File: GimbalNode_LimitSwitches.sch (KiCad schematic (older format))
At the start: 22 parts, among them P4 CONN_01X08_2MNT, P5 CONN_01X08_2MNT, U10 MAX3232CDR, U7 MAX3232CDR, U8 MAX3232CDR, U9 MAX3232CDR

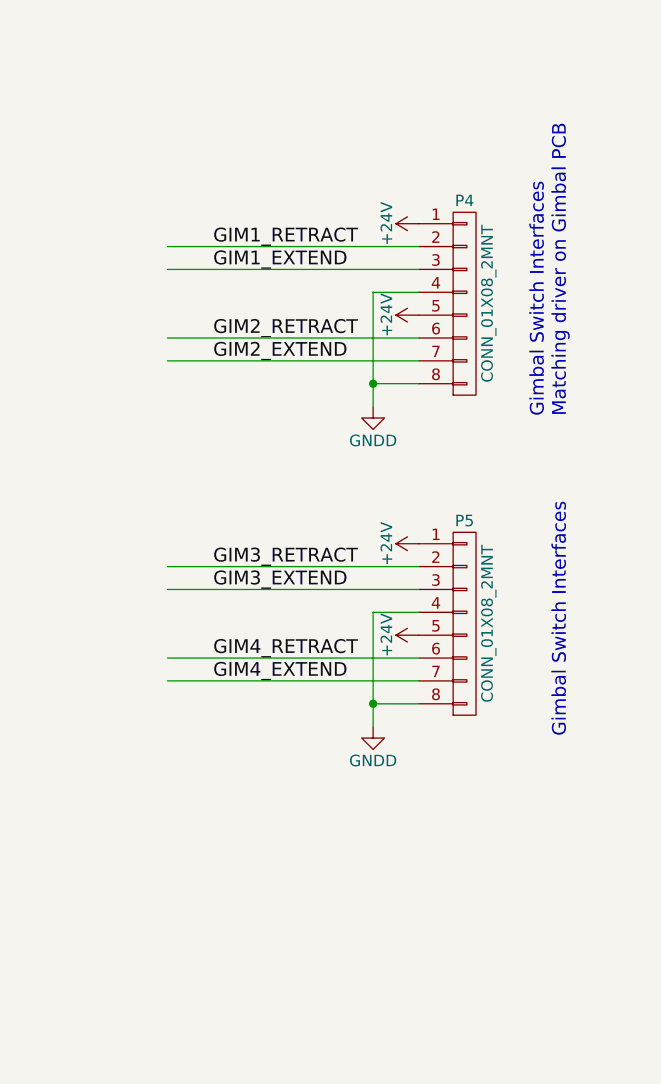
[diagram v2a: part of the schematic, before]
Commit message: Update connectors, diodes, add zener's and anotate.
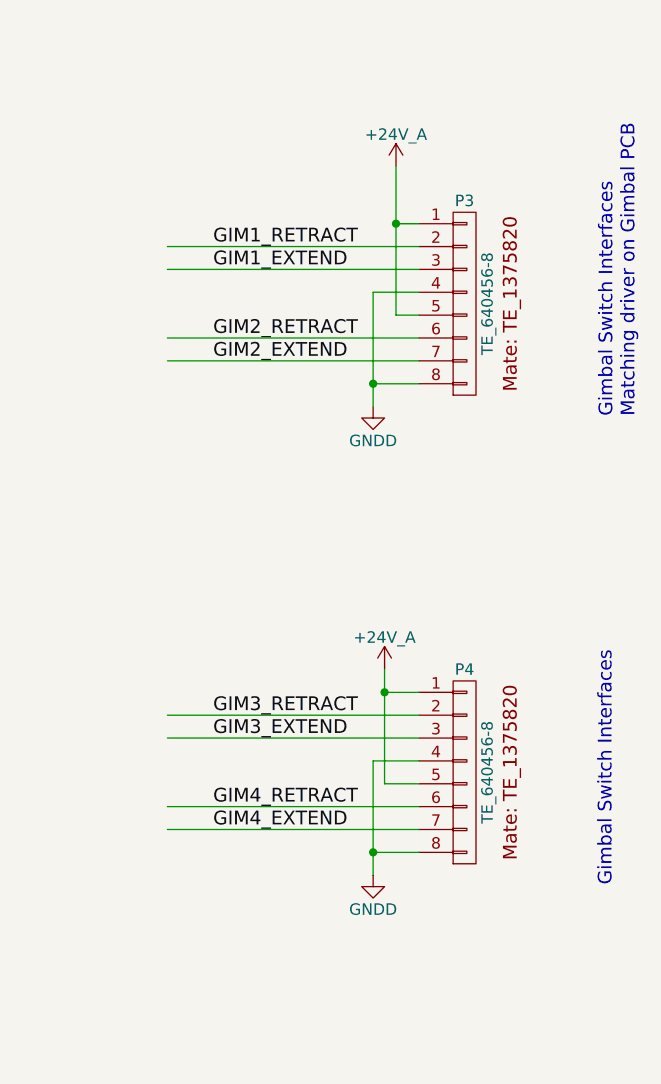
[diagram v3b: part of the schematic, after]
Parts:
- removed P4, P5: CONN_01X08_2MNT, symbol CONN_01X08_2MNT
- added P3, P4: TE_640456-8, RLOOP_FOOTPRINTS:rLoop_TE640456-8, symbol TE_640456-8
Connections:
- net labels added: +24V_A
- net labels removed: +24V
- wire segments 74 -> 80
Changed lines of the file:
@@
 $Descr A3 16535 11693
 encoding utf-8
-Sheet 5 6
+Sheet 4 6
 Title "Gimbal Switch Interface"
 Date ""
@@
 GIM1_EXTEND
 $Comp
-L GNDD #PWR66
+L GNDD #PWR046
 U 1 1 5757EC67
 P 3500 4650
-F 0 "#PWR66" H 3500 4400 50  0001 C CNN
+F 0 "#PWR046" H 3500 4400 50  0001 C CNN
 F 1 "GNDD" H 3500 4500 50  0000 C CNN
 F 2 "" H 3500 4650 50  0000 C CNN
@@
 	3850 4650 3850 4350
 $Comp
-L +3V3_A #PWR65
+L +3V3_A #PWR047
 U 1 1 5757EC68
 P 3500 2000
-F 0 "#PWR65" H 3500 1850 50  0001 C CNN
+F 0 "#PWR047" H 3500 1850 50  0001 C CNN
 F 1 "+3V3_A" H 3500 2140 50  0000 C CNN
 F 2 "" H 3500 2000 60  0000 C CNN
@@
 	2750 3200 2750 3000
 $Comp
-L GNDD #PWR63
+L GNDD #PWR048
 U 1 1 5757EC69
 P 3150 3450
-F 0 "#PWR63" H 3150 3200 50  0001 C CNN
+F 0 "#PWR048" H 3150 3200 50  0001 C CNN
 F 1 "GNDD" H 3150 3300 50  0000 C CNN
 F 2 "" H 3150 3450 50  0000 C CNN
@@
 Wire Wire Line
 	3150 3450 3150 3550
-$Comp
-L CONN_01X08_2MNT P4
-U 1 1 5757EC6A
-P 14300 1850
-F 0 "P4" H 14300 2300 50  0000 C CNN
-F 1 "CONN_01X08_2MNT" V 14400 1850 50  0000 C CNN
-F 2 "" H 14300 1850 50  0000 C CNN
-F 3 "" H 14300 1850 50  0000 C CNN
-	1    14300 1850
-	1    0    0    -1
-$EndComp
-Text Notes 14750 2350 1    60   ~ 0
+Text Notes 15050 2350 1    60   ~ 0
 Gimbal Switch Interfaces\nMatching driver on Gimbal PCB
 $Comp
-L +24V #PWR77
-U 1 1 5757EC6B
-P 14100 1500
-F 0 "#PWR77" H 14100 1350 50  0001 C CNN
-F 1 "+24V" H 14100 1640 50  0000 C CNN
-F 2 "" H 14100 1500 50  0000 C CNN
-F 3 "" H 14100 1500 50  0000 C CNN
-	1    14100 1500
-	0    -1   -1   0
-$EndComp
-$Comp
-L +24V #PWR78
-U 1 1 5757EC6C
-P 14100 1900
-F 0 "#PWR78" H 14100 1750 50  0001 C CNN
-F 1 "+24V" H 14100 2040 50  0000 C CNN
-F 2 "" H 14100 1900 50  0000 C CNN
-F 3 "" H 14100 1900 50  0000 C CNN
-	1    14100 1900
-	0    -1   -1   0
-$EndComp
-$Comp
-L GNDD #PWR75
+L GNDD #PWR049
 U 1 1 5757EC6D
 P 13900 2300
-F 0 "#PWR75" H 13900 2050 50  0001 C CNN
+F 0 "#PWR049" H 13900 2050 50  0001 C CNN
 F 1 "GNDD" H 13900 2150 50  0000 C CNN
 F 2 "" H 13900 2300 50  0000 C CNN
@@
 Text Label 13200 2100 0    60   ~ 0
 GIM2_EXTEND
-$Comp
-L CONN_01X08_2MNT P5
-U 1 1 5757EC6E
-P 14300 3250
-F 0 "P5" H 14300 3700 50  0000 C CNN
-F 1 "CONN_01X08_2MNT" V 14400 3250 50  0000 C CNN
-F 2 "" H 14300 3250 50  0000 C CNN
-F 3 "" H 14300 3250 50  0000 C CNN
-	1    14300 3250
-	1    0    0    -1
-$EndComp
-Text Notes 14750 3750 1    60   ~ 0
+Text Notes 14950 4400 1    60   ~ 0
 Gimbal Switch Interfaces
 $Comp
-L +24V #PWR79
-U 1 1 5757EC6F
-P 14100 2900
-F 0 "#PWR79" H 14100 2750 50  0001 C CNN
-F 1 "+24V" H 14100 3040 50  0000 C CNN
-F 2 "" H 14100 2900 50  0000 C CNN
-F 3 "" H 14100 2900 50  0000 C CNN
-	1    14100 2900
-	0    -1   -1   0
-$EndComp
-$Comp
-L +24V #PWR80
-U 1 1 5757EC70
-P 14100 3300
-F 0 "#PWR80" H 14100 3150 50  0001 C CNN
-F 1 "+24V" H 14100 3440 50  0000 C CNN
-F 2 "" H 14100 3300 50  0000 C CNN
-F 3 "" H 14100 3300 50  0000 C CNN
-	1    14100 3300
-	0    -1   -1   0
-$EndComp
-$Comp
-L GNDD #PWR76
+L GNDD #PWR050
 U 1 1 5757EC71
-P 13900 3700
-F 0 "#PWR76" H 13900 3450 50  0001 C CNN
-F 1 "GNDD" H 13900 3550 50  0000 C CNN
-F 2 "" H 13900 3700 50  0000 C CNN
-F 3 "" H 13900 3700 50  0000 C CNN
-	1    13900 3700
-	1    0    0    -1
-$EndComp
-Wire Wire Line
-	14100 3200 13900 3200
-Wire Wire Line
-	13900 3200 13900 3700
-Wire Wire Line
-	14100 3600 13900 3600
-Connection ~ 13900 3600
-Wire Wire Line
-	13000 3000 14100 3000
-Text Label 13200 3000 0    60   ~ 0
+P 13900 4350
+F 0 "#PWR050" H 13900 4100 50  0001 C CNN
+F 1 "GNDD" H 13900 4200 50  0000 C CNN
+F 2 "" H 13900 4350 50  0000 C CNN
+F 3 "" H 13900 4350 50  0000 C CNN
+	1    13900 4350
+	1    0    0    -1
+$EndComp
+Wire Wire Line
+	14100 3850 13900 3850
+Wire Wire Line
+	13900 3850 13900 4350
+Wire Wire Line
+	14100 4250 13900 4250
+Connection ~ 13900 4250
+Wire Wire Line
+	13000 3650 14100 3650
+Text Label 13200 3650 0    60   ~ 0
 GIM3_RETRACT
 Wire Wire Line
-	13000 3100 14100 3100
-Text Label 13200 3100 0    60   ~ 0
+	13000 3750 14100 3750
+Text Label 13200 3750 0    60   ~ 0
 GIM3_EXTEND
 Wire Wire Line
-	13000 3400 14100 3400
-Text Label 13200 3400 0    60   ~ 0
+	13000 4050 14100 4050
+Text Label 13200 4050 0    60   ~ 0
 GIM4_RETRACT
 Wire Wire Line
-	13000 3500 14100 3500
-Text Label 13200 3500 0    60   ~ 0
+	13000 4150 14100 4150
+Text Label 13200 4150 0    60   ~ 0
 GIM4_EXTEND
 Text HLabel 2800 3650 0    60   Output ~ 0
@@
 GIM2_EXTEND
 $Comp
-L GNDD #PWR68
+L GNDD #PWR051
 U 1 1 5757EC77
 P 3500 7950
-F 0 "#PWR68" H 3500 7700 50  0001 C CNN
+F 0 "#PWR051" H 3500 7700 50  0001 C CNN
 F 1 "GNDD" H 3500 7800 50  0000 C CNN
 F 2 "" H 3500 7950 50  0000 C CNN
@@
 	3850 7950 3850 7650
 $Comp
-L +3V3_A #PWR67
+L +3V3_A #PWR052
 U 1 1 5757EC78
 P 3500 5300
-F 0 "#PWR67" H 3500 5150 50  0001 C CNN
+F 0 "#PWR052" H 3500 5150 50  0001 C CNN
 F 1 "+3V3_A" H 3500 5440 50  0000 C CNN
 F 2 "" H 3500 5300 60  0000 C CNN
@@
 	2750 6500 2750 6300
 $Comp
-L GNDD #PWR64
+L GNDD #PWR053
 U 1 1 5757EC79
 P 3150 6750
-F 0 "#PWR64" H 3150 6500 50  0001 C CNN
+F 0 "#PWR053" H 3150 6500 50  0001 C CNN
 F 1 "GNDD" H 3150 6600 50  0000 C CNN
 F 2 "" H 3150 6750 50  0000 C CNN
@@
 GIM3_EXTEND
 $Comp
-L GNDD #PWR72
+L GNDD #PWR054
 U 1 1 5757EC7F
 P 8700 4650
-F 0 "#PWR72" H 8700 4400 50  0001 C CNN
+F 0 "#PWR054" H 8700 4400 50  0001 C CNN
 F 1 "GNDD" H 8700 4500 50  0000 C CNN
 F 2 "" H 8700 4650 50  0000 C CNN
@@
 	9050 4650 9050 4350
 $Comp
-L +3V3_A #PWR71
+L +3V3_A #PWR055
 U 1 1 5757EC80
 P 8700 2000
-F 0 "#PWR71" H 8700 1850 50  0001 C CNN
+F 0 "#PWR055" H 8700 1850 50  0001 C CNN
 F 1 "+3V3_A" H 8700 2140 50  0000 C CNN
 F 2 "" H 8700 2000 60  0000 C CNN
@@
 	7950 3200 7950 3000
 $Comp
-L GNDD #PWR69
+L GNDD #PWR056
 U 1 1 5757EC81
 P 8350 3450
-F 0 "#PWR69" H 8350 3200 50  0001 C CNN
+F 0 "#PWR056" H 8350 3200 50  0001 C CNN
 F 1 "GNDD" H 8350 3300 50  0000 C CNN
 F 2 "" H 8350 3450 50  0000 C CNN
@@
 GIM4_EXTEND
 $Comp
-L GNDD #PWR74
+L GNDD #PWR057
 U 1 1 5757EC87
 P 8700 7950
-F 0 "#PWR74" H 8700 7700 50  0001 C CNN
+F 0 "#PWR057" H 8700 7700 50  0001 C CNN
 F 1 "GNDD" H 8700 7800 50  0000 C CNN
 F 2 "" H 8700 7950 50  0000 C CNN
@@
 	9050 7950 9050 7650
 $Comp
-L +3V3_A #PWR73
+L +3V3_A #PWR058
 U 1 1 5757EC88
 P 8700 5300
-F 0 "#PWR73" H 8700 5150 50  0001 C CNN
+F 0 "#PWR058" H 8700 5150 50  0001 C CNN
 F 1 "+3V3_A" H 8700 5440 50  0000 C CNN
 F 2 "" H 8700 5300 60  0000 C CNN
@@
 	7950 6500 7950 6300
 $Comp
-L GNDD #PWR70
+L GNDD #PWR059
 U 1 1 5757EC89
 P 8350 6750
-F 0 "#PWR70" H 8350 6500 50  0001 C CNN
+F 0 "#PWR059" H 8350 6500 50  0001 C CNN
 F 1 "GNDD" H 8350 6600 50  0000 C CNN
 F 2 "" H 8350 6750 50  0000 C CNN
@@
 	1    0    0    -1
 $EndComp
+$Comp
+L +24V_A #PWR060
+U 1 1 575C0746
+P 14000 1250
+F 0 "#PWR060" H 14000 1100 50  0001 C CNN
+F 1 "+24V_A" H 14000 1390 50  0000 C CNN
+F 2 "" H 14000 1250 60  0000 C CNN
+F 3 "" H 14000 1250 60  0000 C CNN
+	1    14000 1250
+	1    0    0    -1
+$EndComp
+Wire Wire Line
+	14000 1250 14000 1900
+Wire Wire Line
+	14000 1900 14100 1900
+Wire Wire Line
+	14100 1500 14000 1500
+Connection ~ 14000 1500
+$Comp
+L +24V_A #PWR061
+U 1 1 575C091C
+P 13950 3450
+F 0 "#PWR061" H 13950 3300 50  0001 C CNN
+F 1 "+24V_A" H 13950 3590 50  0000 C CNN
+F 2 "" H 13950 3450 60  0000 C CNN
+F 3 "" H 13950 3450 60  0000 C CNN
+	1    13950 3450
+	1    0    0    -1
+$EndComp
+Wire Wire Line
+	13950 3450 13950 3950
+Wire Wire Line
+	13950 3950 14100 3950
+Wire Wire Line
+	14100 3550 13950 3550
+Connection ~ 13950 3550
+$Comp
+L TE_640456-8 P3
+U 1 1 575C5623
+P 14250 1450
+F 0 "P3" H 14300 1500 50  0000 C CNN
+F 1 "TE_640456-8" V 14400 1050 50  0000 C CNN
+F 2 "RLOOP_FOOTPRINTS:rLoop_TE640456-8" H 14300 1050 50  0001 C CNN
+F 3 "" H 14300 1050 50  0000 C CNN
+	1    14250 1450
+	1    0    0    -1
+$EndComp
+$Comp
+L TE_640456-8 P4
+U 1 1 575C569C
+P 14250 3500
+F 0 "P4" H 14300 3550 50  0000 C CNN
+F 1 "TE_640456-8" V 14400 3100 50  0000 C CNN
+F 2 "RLOOP_FOOTPRINTS:rLoop_TE640456-8" H 14300 3100 50  0001 C CNN
+F 3 "" H 14300 3100 50  0000 C CNN
+	1    14250 3500
+	1    0    0    -1
+$EndComp
